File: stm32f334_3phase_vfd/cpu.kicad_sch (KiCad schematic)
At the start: 13 parts, among them U101 STM32F334K6Tx

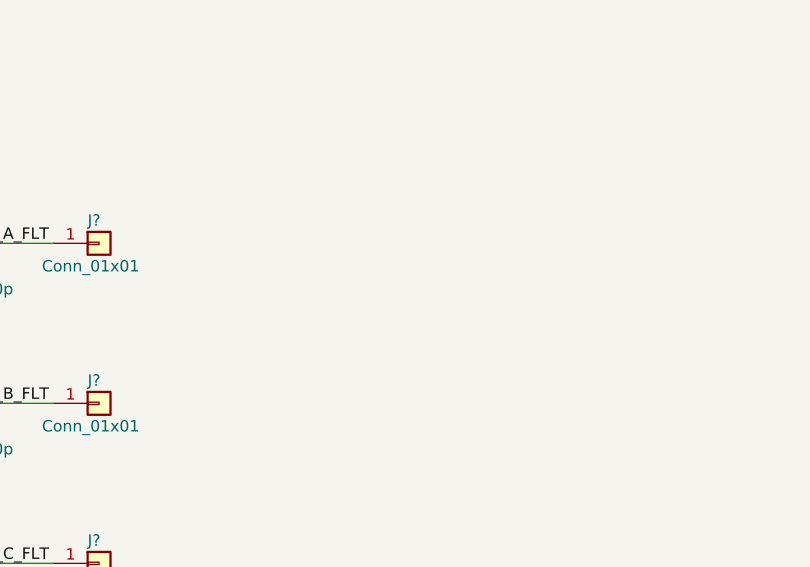
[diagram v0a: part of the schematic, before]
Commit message: update schematic
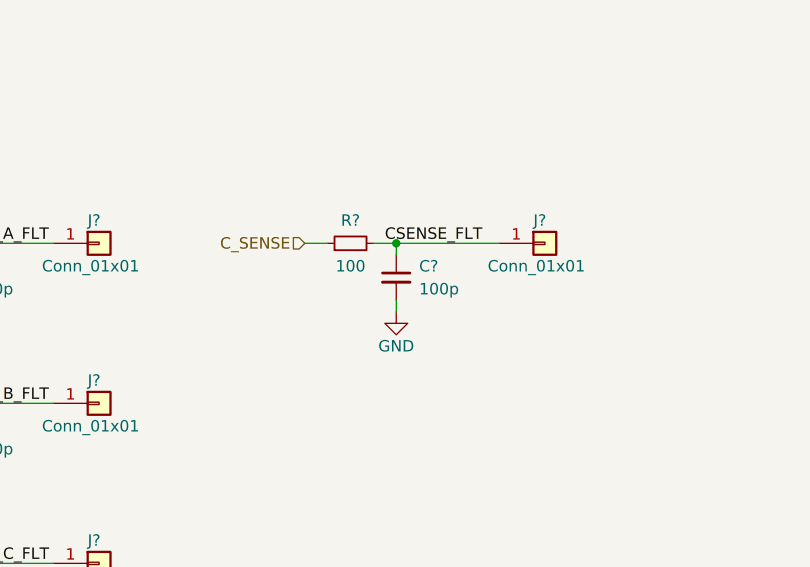
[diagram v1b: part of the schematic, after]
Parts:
- added C?: 100p, symbol Device:C_Small
- added J?: Conn_01x01, symbol Connector_Generic:Conn_01x01
- added R?: 100, symbol Device:R_Small
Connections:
- net GND: now also C?.2
- new net CSENSE_FLT: C?.1, J?.1 (Pin_1), R?.2
- new net C_SENSE: R?.1
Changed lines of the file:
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@@
   (junction (at 35.56 182.88) (diameter 0) (color 0 0 0 0)
   )
+  (junction (at 85.09 147.32) (diameter 0) (color 0 0 0 0)
+  )
   (junction (at 35.56 165.1) (diameter 0) (color 0 0 0 0)
   )
@@
     (stroke (width 0) (type default) (color 0 0 0 0))
   )
+  (wire (pts (xy 82.55 147.32) (xy 85.09 147.32))
+    (stroke (width 0) (type default) (color 0 0 0 0))
+  )
   (wire (pts (xy 35.56 165.1) (xy 35.56 166.37))
     (stroke (width 0) (type default) (color 0 0 0 0))
@@
     (stroke (width 0) (type default) (color 0 0 0 0))
   )
+  (wire (pts (xy 85.09 153.67) (xy 85.09 154.94))
+    (stroke (width 0) (type default) (color 0 0 0 0))
+  )
   (wire (pts (xy 82.55 96.52) (xy 82.55 83.82))
     (stroke (width 0) (type default) (color 0 0 0 0))
@@
     (stroke (width 0) (type default) (color 0 0 0 0))
   )
+  (wire (pts (xy 85.09 147.32) (xy 85.09 148.59))
+    (stroke (width 0) (type default) (color 0 0 0 0))
+  )
   (wire (pts (xy 88.9 83.82) (xy 91.44 83.82))
     (stroke (width 0) (type default) (color 0 0 0 0))
@@
     (stroke (width 0) (type default) (color 0 0 0 0))
   )
+  (wire (pts (xy 74.93 147.32) (xy 77.47 147.32))
+    (stroke (width 0) (type default) (color 0 0 0 0))
+  )
+  (wire (pts (xy 85.09 147.32) (xy 96.52 147.32))
+    (stroke (width 0) (type default) (color 0 0 0 0))
+  )
   (wire (pts (xy 35.56 182.88) (xy 35.56 184.15))
     (stroke (width 0) (type default) (color 0 0 0 0))
+  )
+  (label "CSENSE_FLT" (at 83.82 147.32 0)
+    (effects (font (size 1.27 1.27)) (justify left bottom))
   )
   (label "ISENSE_C_FLT" (at 34.29 182.88 0)
@@
     (effects (font (size 1.27 1.27)) (justify right))
   )
+  (hierarchical_label "C_SENSE" (shape input) (at 74.93 147.32 180)
+    (effects (font (size 1.27 1.27)) (justify right))
+  )
   (hierarchical_label "CPU_3V3" (shape input) (at 27.94 19.05 180)
     (effects (font (size 1.27 1.27)) (justify right))
@@
   (hierarchical_label "L_U" (shape output) (at 267.97 53.34 0)
     (effects (font (size 1.27 1.27)) (justify left))
+  )
+  (symbol (lib_id "Connector_Generic:Conn_01x01") (at 101.6 147.32 0) (unit 1)
+    (in_bom yes) (on_board yes)
+    (property "Reference" "J?" (id 0) (at 100.33 144.78 0)
+      (effects (font (size 1.27 1.27)) (justify left))
+    )
+    (property "Value" "Conn_01x01" (id 1) (at 95.25 149.86 0)
+      (effects (font (size 1.27 1.27)) (justify left))
+    )
+    (property "Footprint" "" (id 2) (at 101.6 147.32 0)
+      (effects (font (size 1.27 1.27)) hide)
+    )
+    (property "Datasheet" "~" (id 3) (at 101.6 147.32 0)
+      (effects (font (size 1.27 1.27)) hide)
+    )
+    (pin "1")
+  )
+  (symbol (lib_id "Device:C_Small") (at 85.09 151.13 0) (unit 1)
+    (in_bom yes) (on_board yes) (fields_autoplaced)
+    (property "Reference" "C?" (id 0) (at 87.63 149.8662 0)
+      (effects (font (size 1.27 1.27)) (justify left))
+    )
+    (property "Value" "100p" (id 1) (at 87.63 152.4062 0)
+      (effects (font (size 1.27 1.27)) (justify left))
+    )
+    (property "Footprint" "" (id 2) (at 85.09 151.13 0)
+      (effects (font (size 1.27 1.27)) hide)
+    )
+    (property "Datasheet" "~" (id 3) (at 85.09 151.13 0)
+      (effects (font (size 1.27 1.27)) hide)
+    )
+    (pin "1")
+    (pin "2")
   )
   (symbol (lib_id "power:GND") (at 35.56 154.94 0) (unit 1)
@@
     )
     (property "Datasheet" "~" (id 3) (at 86.36 96.52 0)
+      (effects (font (size 1.27 1.27)) hide)
+    )
+    (pin "1")
+    (pin "2")
+  )
+  (symbol (lib_id "Device:R_Small") (at 80.01 147.32 90) (unit 1)
+    (in_bom yes) (on_board yes)
+    (property "Reference" "R?" (id 0) (at 80.01 144.78 90))
+    (property "Value" "100" (id 1) (at 80.01 149.86 90))
+    (property "Footprint" "" (id 2) (at 80.01 147.32 0)
+      (effects (font (size 1.27 1.27)) hide)
+    )
+    (property "Datasheet" "~" (id 3) (at 80.01 147.32 0)
       (effects (font (size 1.27 1.27)) hide)
     )
@@
     (pin "9")
   )
+  (symbol (lib_id "power:GND") (at 85.09 154.94 0) (unit 1)
+    (in_bom yes) (on_board yes)
+    (property "Reference" "#PWR?" (id 0) (at 85.09 161.29 0)
+      (effects (font (size 1.27 1.27)) hide)
+    )
+    (property "Value" "GND" (id 1) (at 85.09 158.75 0))
+    (property "Footprint" "" (id 2) (at 85.09 154.94 0)
+      (effects (font (size 1.27 1.27)) hide)
+    )
+    (property "Datasheet" "" (id 3) (at 85.09 154.94 0)
+      (effects (font (size 1.27 1.27)) hide)
+    )
+    (pin "1")
+  )
   (symbol (lib_id "Device:C_Small") (at 86.36 83.82 90) (unit 1)

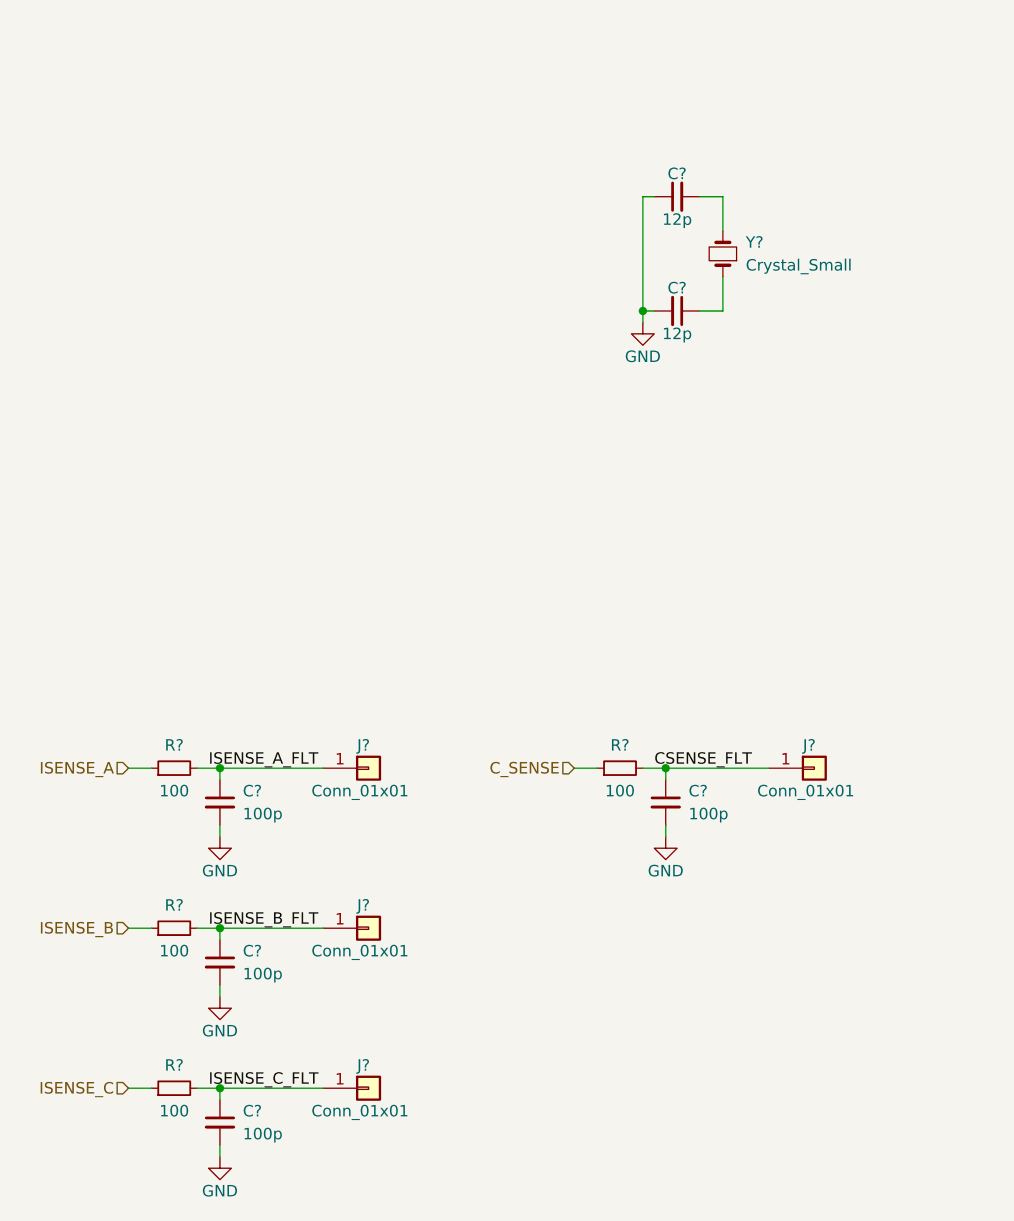
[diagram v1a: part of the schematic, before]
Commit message: update schematic, start power section layout
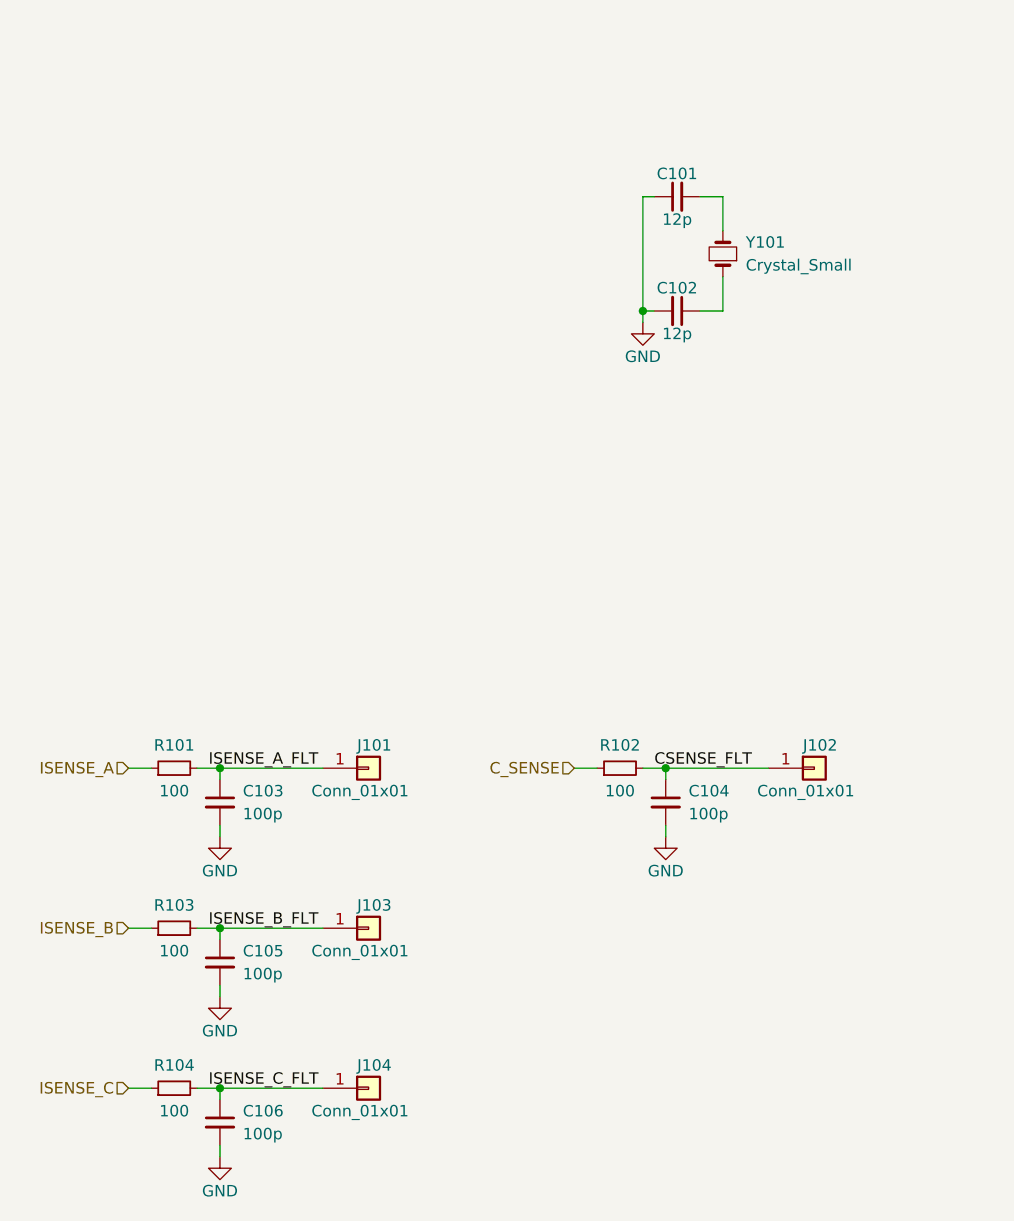
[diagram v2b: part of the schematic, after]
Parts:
- gave numbers to parts that had none: 15
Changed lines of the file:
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@@
   (symbol (lib_id "Connector_Generic:Conn_01x01") (at 101.6 147.32 0) (unit 1)
     (in_bom yes) (on_board yes)
-    (property "Reference" "J?" (id 0) (at 100.33 144.78 0)
+    (property "Reference" "J102" (id 0) (at 100.33 144.78 0)
       (effects (font (size 1.27 1.27)) (justify left))
     )
@@
   (symbol (lib_id "Device:C_Small") (at 85.09 151.13 0) (unit 1)
     (in_bom yes) (on_board yes) (fields_autoplaced)
-    (property "Reference" "C?" (id 0) (at 87.63 149.8662 0)
+    (property "Reference" "C104" (id 0) (at 87.63 149.8662 0)
       (effects (font (size 1.27 1.27)) (justify left))
     )
@@
   (symbol (lib_id "power:GND") (at 35.56 154.94 0) (unit 1)
     (in_bom yes) (on_board yes)
-    (property "Reference" "#PWR?" (id 0) (at 35.56 161.29 0)
+    (property "Reference" "#PWR0103" (id 0) (at 35.56 161.29 0)
       (effects (font (size 1.27 1.27)) hide)
     )
@@
   (symbol (lib_id "power:GND") (at 151.13 119.38 0) (unit 1)
     (in_bom yes) (on_board yes)
-    (property "Reference" "#PWR?" (id 0) (at 151.13 125.73 0)
+    (property "Reference" "#PWR0102" (id 0) (at 151.13 125.73 0)
       (effects (font (size 1.27 1.27)) hide)
     )
@@
   (symbol (lib_id "Device:C_Small") (at 35.56 186.69 0) (unit 1)
     (in_bom yes) (on_board yes) (fields_autoplaced)
-    (property "Reference" "C?" (id 0) (at 38.1 185.4262 0)
+    (property "Reference" "C106" (id 0) (at 38.1 185.4262 0)
       (effects (font (size 1.27 1.27)) (justify left))
     )
@@
   (symbol (lib_id "Device:C_Small") (at 35.56 151.13 0) (unit 1)
     (in_bom yes) (on_board yes) (fields_autoplaced)
-    (property "Reference" "C?" (id 0) (at 38.1 149.8662 0)
+    (property "Reference" "C103" (id 0) (at 38.1 149.8662 0)
       (effects (font (size 1.27 1.27)) (justify left))
     )
@@
   (symbol (lib_id "Device:C_Small") (at 86.36 96.52 270) (unit 1)
     (in_bom yes) (on_board yes)
-    (property "Reference" "C?" (id 0) (at 86.36 93.98 90))
+    (property "Reference" "C102" (id 0) (at 86.36 93.98 90))
     (property "Value" "12p" (id 1) (at 86.36 99.06 90))
     (property "Footprint" "" (id 2) (at 86.36 96.52 0)
@@
   (symbol (lib_id "Device:R_Small") (at 80.01 147.32 90) (unit 1)
     (in_bom yes) (on_board yes)
-    (property "Reference" "R?" (id 0) (at 80.01 144.78 90))
+    (property "Reference" "R102" (id 0) (at 80.01 144.78 90))
     (property "Value" "100" (id 1) (at 80.01 149.86 90))
     (property "Footprint" "" (id 2) (at 80.01 147.32 0)
@@
   (symbol (lib_id "Device:R_Small") (at 30.48 182.88 90) (unit 1)
     (in_bom yes) (on_board yes)
-    (property "Reference" "R?" (id 0) (at 30.48 180.34 90))
+    (property "Reference" "R104" (id 0) (at 30.48 180.34 90))
     (property "Value" "100" (id 1) (at 30.48 185.42 90))
     (property "Footprint" "" (id 2) (at 30.48 182.88 0)
@@
   (symbol (lib_id "Device:R_Small") (at 30.48 165.1 90) (unit 1)
     (in_bom yes) (on_board yes)
-    (property "Reference" "R?" (id 0) (at 30.48 162.56 90))
+    (property "Reference" "R103" (id 0) (at 30.48 162.56 90))
     (property "Value" "100" (id 1) (at 30.48 167.64 90))
     (property "Footprint" "" (id 2) (at 30.48 165.1 0)
@@
   (symbol (lib_id "Connector_Generic:Conn_01x01") (at 52.07 147.32 0) (unit 1)
     (in_bom yes) (on_board yes)
-    (property "Reference" "J?" (id 0) (at 50.8 144.78 0)
+    (property "Reference" "J101" (id 0) (at 50.8 144.78 0)
       (effects (font (size 1.27 1.27)) (justify left))
     )
@@
   (symbol (lib_id "power:GND") (at 35.56 172.72 0) (unit 1)
     (in_bom yes) (on_board yes)
-    (property "Reference" "#PWR?" (id 0) (at 35.56 179.07 0)
+    (property "Reference" "#PWR0105" (id 0) (at 35.56 179.07 0)
       (effects (font (size 1.27 1.27)) hide)
     )
@@
   (symbol (lib_id "Device:C_Small") (at 35.56 168.91 0) (unit 1)
     (in_bom yes) (on_board yes) (fields_autoplaced)
-    (property "Reference" "C?" (id 0) (at 38.1 167.6462 0)
+    (property "Reference" "C105" (id 0) (at 38.1 167.6462 0)
       (effects (font (size 1.27 1.27)) (justify left))
     )
@@
   (symbol (lib_id "power:GND") (at 35.56 190.5 0) (unit 1)
     (in_bom yes) (on_board yes)
-    (property "Reference" "#PWR?" (id 0) (at 35.56 196.85 0)
+    (property "Reference" "#PWR0106" (id 0) (at 35.56 196.85 0)
       (effects (font (size 1.27 1.27)) hide)
     )
@@
   (symbol (lib_id "Connector_Generic:Conn_01x01") (at 52.07 182.88 0) (unit 1)
     (in_bom yes) (on_board yes)
-    (property "Reference" "J?" (id 0) (at 50.8 180.34 0)
+    (property "Reference" "J104" (id 0) (at 50.8 180.34 0)
       (effects (font (size 1.27 1.27)) (justify left))
     )
@@
   (symbol (lib_id "power:GND") (at 85.09 154.94 0) (unit 1)
     (in_bom yes) (on_board yes)
-    (property "Reference" "#PWR?" (id 0) (at 85.09 161.29 0)
+    (property "Reference" "#PWR0104" (id 0) (at 85.09 161.29 0)
       (effects (font (size 1.27 1.27)) hide)
     )
@@
   (symbol (lib_id "Device:C_Small") (at 86.36 83.82 90) (unit 1)
     (in_bom yes) (on_board yes)
-    (property "Reference" "C?" (id 0) (at 86.36 81.28 90))
+    (property "Reference" "C101" (id 0) (at 86.36 81.28 90))
     (property "Value" "12p" (id 1) (at 86.36 86.36 90))
     (property "Footprint" "" (id 2) (at 86.36 83.82 0)
@@
   (symbol (lib_id "power:GND") (at 82.55 97.79 0) (unit 1)
     (in_bom yes) (on_board yes)
-    (property "Reference" "#PWR?" (id 0) (at 82.55 104.14 0)
+    (property "Reference" "#PWR0101" (id 0) (at 82.55 104.14 0)
       (effects (font (size 1.27 1.27)) hide)
     )
@@
   (symbol (lib_id "Device:R_Small") (at 30.48 147.32 90) (unit 1)
     (in_bom yes) (on_board yes)
-    (property "Reference" "R?" (id 0) (at 30.48 144.78 90))
+    (property "Reference" "R101" (id 0) (at 30.48 144.78 90))
     (property "Value" "100" (id 1) (at 30.48 149.86 90))
     (property "Footprint" "" (id 2) (at 30.48 147.32 0)
@@
   (symbol (lib_id "Connector_Generic:Conn_01x01") (at 52.07 165.1 0) (unit 1)
     (in_bom yes) (on_board yes)
-    (property "Reference" "J?" (id 0) (at 50.8 162.56 0)
+    (property "Reference" "J103" (id 0) (at 50.8 162.56 0)
       (effects (font (size 1.27 1.27)) (justify left))
     )
@@
   (symbol (lib_id "Device:Crystal_Small") (at 91.44 90.17 90) (unit 1)
     (in_bom yes) (on_board yes) (fields_autoplaced)
-    (property "Reference" "Y?" (id 0) (at 93.98 88.8999 90)
+    (property "Reference" "Y101" (id 0) (at 93.98 88.8999 90)
       (effects (font (size 1.27 1.27)) (justify right))
     )
